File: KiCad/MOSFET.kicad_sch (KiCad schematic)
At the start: 0 parts

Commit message: Afegist el MOSFET
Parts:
- added Q1: IRLZ44N, Package_TO_SOT_THT:TO-220-3_Vertical, symbol Transistor_FET:IRLZ44N
- added R1: 3.6, symbol Device:R
- added R2: 100, symbol Device:R
- added R3: 10k, symbol Device:R
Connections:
- new net: Q1.1 (G), R2.2, R3.1
- new net: Q1.2 (D), R1.2
- new net GND: Q1.3 (S), R3.2

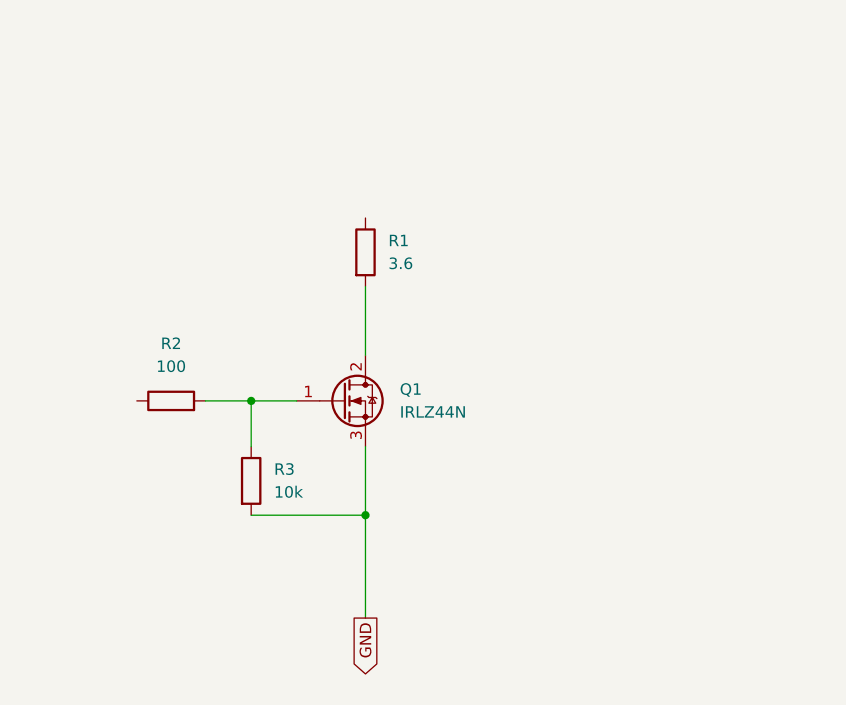
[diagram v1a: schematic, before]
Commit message: Afegist el MOSFET
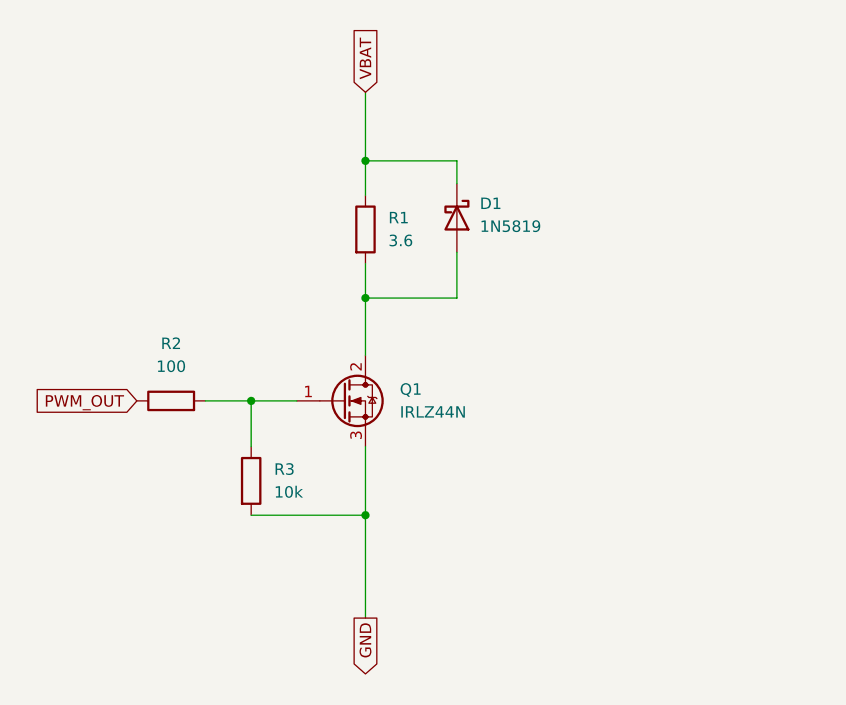
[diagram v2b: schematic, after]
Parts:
- added D1: 1N5819, Diode_THT:D_DO-41_SOD81_P10.16mm_Horizontal, symbol Diode:1N5819
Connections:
- net VBAT: now reaches R1.1
- net VBAT: now also D1.1 (K)
- net at Q1.2 (D), R1.2: now also D1.2 (A)
- net PWM_OUT: now reaches R2.1
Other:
- moved on the sheet: R1
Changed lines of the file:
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@@
 	(paper "A4")
+	(junction
+		(at 146.05 62.23)
+		(diameter 0)
+		(color 0 0 0 0)
+	)
 	(junction
 		(at 146.05 101.6)
@@
 	)
 	(junction
+		(at 146.05 77.47)
+		(diameter 0)
+		(color 0 0 0 0)
+	)
+	(junction
 		(at 133.35 88.9)
 		(diameter 0)
@@
 	(wire
 		(pts
-			(xy 146.05 76.2) (xy 146.05 83.82)
+			(xy 146.05 62.23) (xy 146.05 66.04)
+		)
+		(stroke
+			(width 0)
+			(type default)
+		)
+	)
+	(wire
+		(pts
+			(xy 156.21 72.39) (xy 156.21 77.47)
+		)
+		(stroke
+			(width 0)
+			(type default)
+		)
+	)
+	(wire
+		(pts
+			(xy 146.05 73.66) (xy 146.05 77.47)
+		)
+		(stroke
+			(width 0)
+			(type default)
+		)
+	)
+	(wire
+		(pts
+			(xy 146.05 54.61) (xy 146.05 62.23)
 		)
 		(stroke
@@
 	(wire
 		(pts
+			(xy 146.05 77.47) (xy 146.05 83.82)
+		)
+		(stroke
+			(width 0)
+			(type default)
+		)
+	)
+	(wire
+		(pts
 			(xy 133.35 101.6) (xy 146.05 101.6)
 		)
@@
 		(pts
 			(xy 146.05 101.6) (xy 146.05 113.03)
+		)
+		(stroke
+			(width 0)
+			(type default)
+		)
+	)
+	(wire
+		(pts
+			(xy 156.21 77.47) (xy 146.05 77.47)
+		)
+		(stroke
+			(width 0)
+			(type default)
+		)
+	)
+	(wire
+		(pts
+			(xy 156.21 62.23) (xy 146.05 62.23)
+		)
+		(stroke
+			(width 0)
+			(type default)
+		)
+	)
+	(wire
+		(pts
+			(xy 156.21 64.77) (xy 156.21 62.23)
 		)
 		(stroke
@@
 		(property "Intersheetrefs" "${INTERSHEET_REFS}"
 			(at 146.05 119.8857 90)
+			(effects
+				(font
+					(size 1.27 1.27)
+				)
+				(justify right)
+				(hide yes)
+			)
+		)
+	)
+	(global_label "VBAT"
+		(shape input)
+		(at 146.05 54.61 90)
+		(fields_autoplaced yes)
+		(effects
+			(font
+				(size 1.27 1.27)
+			)
+			(justify left)
+		)
+		(property "Intersheetrefs" "${INTERSHEET_REFS}"
+			(at 146.05 47.8642 90)
+			(effects
+				(font
+					(size 1.27 1.27)
+				)
+				(justify left)
+				(hide yes)
+			)
+		)
+	)
+	(global_label "PWM_OUT"
+		(shape input)
+		(at 120.65 88.9 180)
+		(fields_autoplaced yes)
+		(effects
+			(font
+				(size 1.27 1.27)
+			)
+			(justify right)
+		)
+		(property "Intersheetrefs" "${INTERSHEET_REFS}"
+			(at 108.8958 88.9 0)
 			(effects
 				(font
@@
 	(symbol
 		(lib_id "Device:R")
-		(at 146.05 72.39 0)
+		(at 146.05 69.85 0)
 		(unit 1)
 		(exclude_from_sim no)
@@
 		(fields_autoplaced yes)
 		(property "Reference" "R1"
+			(at 148.59 68.5799 0)
+			(effects
+				(font
+					(size 1.27 1.27)
+				)
+				(justify left)
+			)
+		)
+		(property "Value" "3.6"
 			(at 148.59 71.1199 0)
 			(effects
@@
 			)
 		)
-		(property "Value" "3.6"
-			(at 148.59 73.6599 0)
-			(effects
-				(font
-					(size 1.27 1.27)
-				)
-				(justify left)
-			)
-		)
 		(property "Footprint" ""
-			(at 144.272 72.39 90)
+			(at 144.272 69.85 90)
 			(effects
 				(font
@@
 		)
 		(property "Datasheet" "~"
-			(at 146.05 72.39 0)
+			(at 146.05 69.85 0)
 			(effects
 				(font
@@
 		)
 		(property "Description" "Resistor"
-			(at 146.05 72.39 0)
+			(at 146.05 69.85 0)
 			(effects
 				(font
@@
 					(unit 1)
 				)
+			)
+		)
+	)
+	(symbol
+		(lib_id "Diode:1N5819")
+		(at 156.21 68.58 270)
+		(unit 1)
+		(exclude_from_sim no)
+		(in_bom yes)
+		(on_board yes)
+		(dnp no)
+		(fields_autoplaced yes)
+		(property "Reference" "D1"
+			(at 158.75 66.9924 90)
+			(effects
+				(font
+					(size 1.27 1.27)
+				)
+				(justify left)
+			)
+		)
+		(property "Value" "1N5819"
+			(at 158.75 69.5324 90)
+			(effects
+				(font
+					(size 1.27 1.27)
+				)
+				(justify left)
+			)
+		)
+		(property "Footprint" "Diode_THT:D_DO-41_SOD81_P10.16mm_Horizontal"
+			(at 151.765 68.58 0)
+			(effects
+				(font
+					(size 1.27 1.27)
+				)
+				(hide yes)
+			)
+		)
+		(property "Datasheet" "http://www.vishay.com/docs/88525/1n5817.pdf"
+			(at 156.21 68.58 0)
+			(effects
+				(font
+					(size 1.27 1.27)
+				)
+				(hide yes)
+			)
+		)
+		(property "Description" "40V 1A Schottky Barrier Rectifier Diode, DO-41"
+			(at 156.21 68.58 0)
+			(effects
+				(font
+					(size 1.27 1.27)
+				)
+				(hide yes)
+			)
+		)
+		(pin "1"
+		)
+		(pin "2"
+		)
+		(instances
+			(project ""
+				(path "/6381918b-bb9e-4107-aca1-9c14e5889eac"
+					(reference "D1")
+					(unit 1)
+				)

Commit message: Millora
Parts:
- renumbered D1 to D4, R2 to R15, R3 to R16, R1 to R17
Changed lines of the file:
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@@
 		(dnp no)
 		(fields_autoplaced yes)
-		(property "Reference" "R3"
+		(property "Reference" "R16"
 			(at 135.89 96.5199 0)
 			(effects
@@
 				(path "/6381918b-bb9e-4107-aca1-9c14e5889eac"
 					(reference "R3")
+					(unit 1)
+				)
+			)
+			(project "SEIENTS_EDD"
+				(path "/b6401b4f-5426-49b8-bb2e-8ecdb19989ef/df19026d-ff61-4139-84bd-7b499d6482c5"
+					(reference "R16")
 					(unit 1)
 				)
@@
 		(dnp no)
 		(fields_autoplaced yes)
-		(property "Reference" "R1"
+		(property "Reference" "R17"
 			(at 148.59 68.5799 0)
 			(effects
@@
 				(path "/6381918b-bb9e-4107-aca1-9c14e5889eac"
 					(reference "R1")
+					(unit 1)
+				)
+			)
+			(project "SEIENTS_EDD"
+				(path "/b6401b4f-5426-49b8-bb2e-8ecdb19989ef/df19026d-ff61-4139-84bd-7b499d6482c5"
+					(reference "R17")
 					(unit 1)
 				)
@@
 		(dnp no)
 		(fields_autoplaced yes)
-		(property "Reference" "R2"
+		(property "Reference" "R15"
 			(at 124.46 82.55 90)
 			(effects
@@
 				(path "/6381918b-bb9e-4107-aca1-9c14e5889eac"
 					(reference "R2")
+					(unit 1)
+				)
+			)
+			(project "SEIENTS_EDD"
+				(path "/b6401b4f-5426-49b8-bb2e-8ecdb19989ef/df19026d-ff61-4139-84bd-7b499d6482c5"
+					(reference "R15")
 					(unit 1)
 				)
@@
 		(dnp no)
 		(fields_autoplaced yes)
-		(property "Reference" "D1"
+		(property "Reference" "D4"
 			(at 158.75 66.9924 90)
 			(effects
@@
 				(path "/6381918b-bb9e-4107-aca1-9c14e5889eac"
 					(reference "D1")
+					(unit 1)
+				)
+			)
+			(project "SEIENTS_EDD"
+				(path "/b6401b4f-5426-49b8-bb2e-8ecdb19989ef/df19026d-ff61-4139-84bd-7b499d6482c5"
+					(reference "D4")
 					(unit 1)
 				)
@@
 					(reference "Q1")
 					(unit 1)
+				)
+			)
+			(project "SEIENTS_EDD"
+				(path "/b6401b4f-5426-49b8-bb2e-8ecdb19989ef/df19026d-ff61-4139-84bd-7b499d6482c5"
+					(reference "Q1")
+					(unit 1)

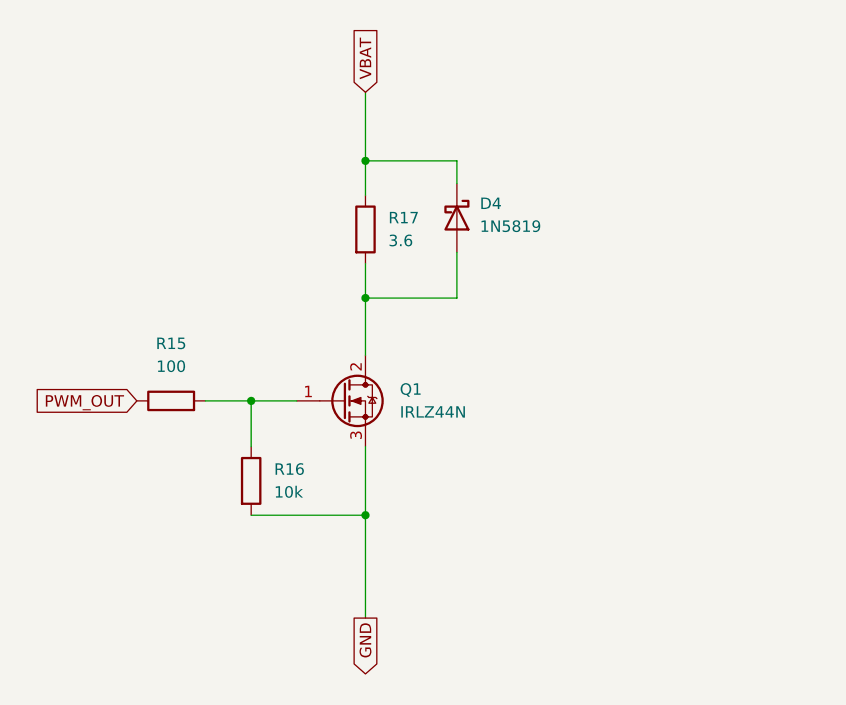
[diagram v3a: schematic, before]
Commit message: cambios mejora ERC
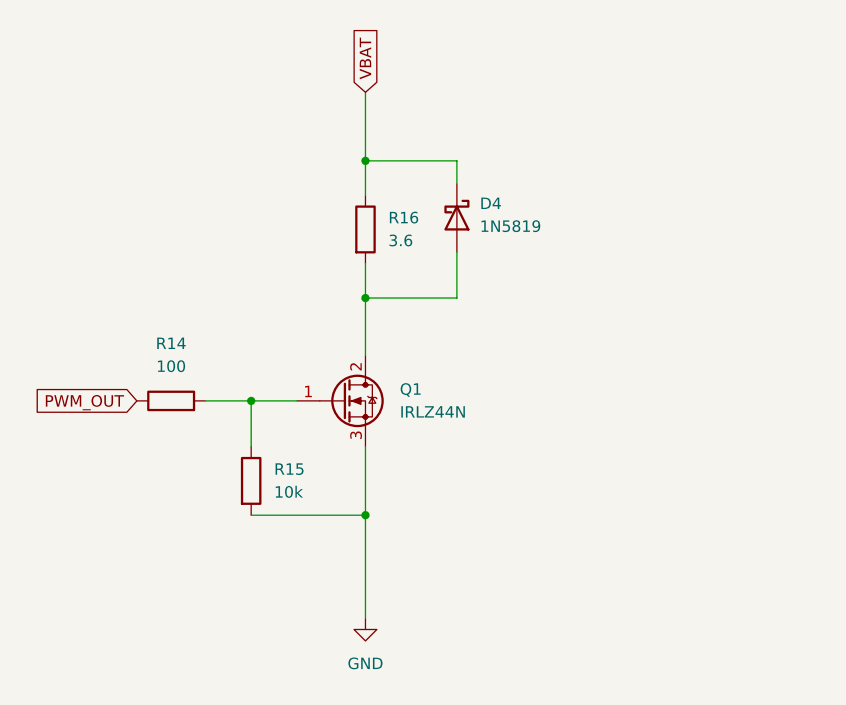
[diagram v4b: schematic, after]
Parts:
- renumbered R15 to R14, R16 to R15, R17 to R16
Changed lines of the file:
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@@
 		)
 	)
-	(global_label "GND"
-		(shape output)
-		(at 146.05 113.03 270)
+	(global_label "VBAT"
+		(shape input)
+		(at 146.05 54.61 90)
 		(fields_autoplaced yes)
 		(effects
@@
 				(size 1.27 1.27)
 			)
-			(justify right)
+			(justify left)
 		)
 		(property "Intersheetrefs" "${INTERSHEET_REFS}"
-			(at 146.05 119.8857 90)
-			(effects
-				(font
-					(size 1.27 1.27)
-				)
-				(justify right)
-				(hide yes)
-			)
-		)
-	)
-	(global_label "VBAT"
+			(at 146.05 47.8642 90)
+			(effects
+				(font
+					(size 1.27 1.27)
+				)
+				(justify left)
+				(hide yes)
+			)
+		)
+	)
+	(global_label "PWM_OUT"
 		(shape input)
-		(at 146.05 54.61 90)
+		(at 120.65 88.9 180)
 		(fields_autoplaced yes)
 		(effects
@@
 				(size 1.27 1.27)
 			)
-			(justify left)
-		)
-		(property "Intersheetrefs" "${INTERSHEET_REFS}"
-			(at 146.05 47.8642 90)
-			(effects
-				(font
-					(size 1.27 1.27)
-				)
-				(justify left)
-				(hide yes)
-			)
-		)
-	)
-	(global_label "PWM_OUT"
-		(shape input)
-		(at 120.65 88.9 180)
-		(fields_autoplaced yes)
-		(effects
-			(font
-				(size 1.27 1.27)
-			)
 			(justify right)
 		)
@@
 		(dnp no)
 		(fields_autoplaced yes)
-		(property "Reference" "R16"
+		(property "Reference" "R15"
 			(at 135.89 96.5199 0)
 			(effects
@@
 			(project "SEIENTS_EDD"
 				(path "/b6401b4f-5426-49b8-bb2e-8ecdb19989ef/df19026d-ff61-4139-84bd-7b499d6482c5"
-					(reference "R16")
+					(reference "R15")
 					(unit 1)
 				)
@@
 		(dnp no)
 		(fields_autoplaced yes)
-		(property "Reference" "R17"
+		(property "Reference" "R16"
 			(at 148.59 68.5799 0)
 			(effects
@@
 			(project "SEIENTS_EDD"
 				(path "/b6401b4f-5426-49b8-bb2e-8ecdb19989ef/df19026d-ff61-4139-84bd-7b499d6482c5"
-					(reference "R17")
+					(reference "R16")
 					(unit 1)
 				)
@@
 		(dnp no)
 		(fields_autoplaced yes)
-		(property "Reference" "R15"
+		(property "Reference" "R14"
 			(at 124.46 82.55 90)
 			(effects
@@
 			(project "SEIENTS_EDD"
 				(path "/b6401b4f-5426-49b8-bb2e-8ecdb19989ef/df19026d-ff61-4139-84bd-7b499d6482c5"
-					(reference "R15")
+					(reference "R14")
 					(unit 1)
 				)
@@
 					(unit 1)
 				)
+			)
+		)
+	)
+	(symbol
+		(lib_id "power:GND")
+		(at 146.05 113.03 0)
+		(unit 1)
+		(exclude_from_sim no)
+		(in_bom yes)
+		(on_board yes)
+		(dnp no)
+		(fields_autoplaced yes)
+		(property "Reference" "#PWR031"
+			(at 146.05 119.38 0)
+			(effects
+				(font
+					(size 1.27 1.27)
+				)
+				(hide yes)
+			)
+		)
+		(property "Value" "GND"
+			(at 146.05 118.11 0)
+			(effects
+				(font
+					(size 1.27 1.27)
+				)
+			)
+		)
+		(property "Footprint" ""
+			(at 146.05 113.03 0)
+			(effects
+				(font
+					(size 1.27 1.27)
+				)
+				(hide yes)
+			)
+		)
+		(property "Datasheet" ""
+			(at 146.05 113.03 0)
+			(effects
+				(font
+					(size 1.27 1.27)
+				)
+				(hide yes)
+			)
+		)
+		(property "Description" "Power symbol creates a global label with name \"GND\" , ground"
+			(at 146.05 113.03 0)
+			(effects
+				(font
+					(size 1.27 1.27)
+				)
+				(hide yes)
+			)
+		)
+		(pin "1"
+		)
+		(instances
+			(project ""
+				(path "/6381918b-bb9e-4107-aca1-9c14e5889eac"
+					(reference "#PWR01")
+					(unit 1)
+				)
+			)
+			(project "SEIENTS_EDD"
+				(path "/b6401b4f-5426-49b8-bb2e-8ecdb19989ef/df19026d-ff61-4139-84bd-7b499d6482c5"
+					(reference "#PWR031")
+					(unit 1)
+				)

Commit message: Modificacions al MOSFET
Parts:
- removed R14: 100, symbol Device:R
- added J66: Screw_Terminal_01x02, symbol Connector:Screw_Terminal_01x02
- R1: renamed from R16; value 3.6 -> 360
- renumbered D4 to D1, R15 to R3
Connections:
- net GND: now also D1.1 (K)
- net VBAT: now also J66.2 (Pin_2); no longer D1.1 (K)
- net CALEFACCIÓ: now reaches Q1.1 (G), R3.1
- net at D1.2 (A), R1.2: no longer Q1.2 (D)
- new net: J66.1 (Pin_1), Q1.2 (D)
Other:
- moved on the sheet: D1, R1

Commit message: Modificacions Micro
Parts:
- renumbered D1 to D4, J66 to J5, R3 to R15, R1 to R22
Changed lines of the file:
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@@
 	(paper "A4")
-	(junction
-		(at 146.05 113.03)
-		(diameter 0)
-		(color 0 0 0 0)
-	)
 	(junction
 		(at 146.05 101.6)
@@
 		(dnp no)
 		(fields_autoplaced yes)
-		(property "Reference" "#PWR02"
+		(property "Reference" "#PWR046"
 			(at 186.69 119.38 0)
 			(effects
@@
 				(path "/6381918b-bb9e-4107-aca1-9c14e5889eac"
 					(reference "#PWR02")
+					(unit 1)
+				)
+			)
+			(project "SEIENTS_EDD"
+				(path "/b6401b4f-5426-49b8-bb2e-8ecdb19989ef/df19026d-ff61-4139-84bd-7b499d6482c5"
+					(reference "#PWR046")
 					(unit 1)
 				)
@@
 		(dnp no)
 		(fields_autoplaced yes)
-		(property "Reference" "R3"
+		(property "Reference" "R15"
 			(at 135.89 96.5199 0)
 			(effects
@@
 		(dnp no)
 		(fields_autoplaced yes)
-		(property "Reference" "R1"
+		(property "Reference" "R22"
 			(at 189.23 91.4399 0)
 			(effects
@@
 				(path "/6381918b-bb9e-4107-aca1-9c14e5889eac"
 					(reference "R1")
+					(unit 1)
+				)
+			)
+			(project "SEIENTS_EDD"
+				(path "/b6401b4f-5426-49b8-bb2e-8ecdb19989ef/df19026d-ff61-4139-84bd-7b499d6482c5"
+					(reference "R22")
 					(unit 1)
 				)
@@
 		(dnp no)
 		(fields_autoplaced yes)
-		(property "Reference" "D1"
+		(property "Reference" "D4"
 			(at 189.23 103.1874 90)
 			(effects
@@
 	)
 	(symbol
-		(lib_id "power:PWR_FLAG")
-		(at 146.05 113.03 90)
-		(unit 1)
-		(exclude_from_sim no)
-		(in_bom yes)
-		(on_board yes)
-		(dnp no)
-		(fields_autoplaced yes)
-		(property "Reference" "#FLG01"
-			(at 144.145 113.03 0)
-			(effects
-				(font
-					(size 1.27 1.27)
-				)
-				(hide yes)
-			)
-		)
-		(property "Value" "PWR_FLAG"
-			(at 142.24 113.0299 90)
-			(effects
-				(font
-					(size 1.27 1.27)
-				)
-				(justify left)
-			)
-		)
-		(property "Footprint" ""
-			(at 146.05 113.03 0)
-			(effects
-				(font
-					(size 1.27 1.27)
-				)
-				(hide yes)
-			)
-		)
-		(property "Datasheet" "~"
-			(at 146.05 113.03 0)
-			(effects
-				(font
-					(size 1.27 1.27)
-				)
-				(hide yes)
-			)
-		)
-		(property "Description" "Special symbol for telling ERC where power comes from"
-			(at 146.05 113.03 0)
-			(effects
-				(font
-					(size 1.27 1.27)
-				)
-				(hide yes)
-			)
-		)
-		(pin "1"
-		)
-		(instances
-			(project ""
-				(path "/6381918b-bb9e-4107-aca1-9c14e5889eac"
-					(reference "#FLG01")
-					(unit 1)
-				)
-			)
-		)
-	)
-	(symbol
 		(lib_id "power:GND")
 		(at 146.05 113.03 0)
@@
 		(dnp no)
 		(fields_autoplaced yes)
-		(property "Reference" "#PWR01"
+		(property "Reference" "#PWR031"
 			(at 146.05 119.38 0)
 			(effects
@@
 		(dnp no)
 		(fields_autoplaced yes)
-		(property "Reference" "J66"
+		(property "Reference" "J5"
 			(at 151.13 71.1199 90)
 			(effects
@@
 					(unit 1)
 				)
+			)
+			(project "SEIENTS_EDD"
+				(path "/b6401b4f-5426-49b8-bb2e-8ecdb19989ef/df19026d-ff61-4139-84bd-7b499d6482c5"
+					(reference "J5")
+					(unit 1)
+				)
